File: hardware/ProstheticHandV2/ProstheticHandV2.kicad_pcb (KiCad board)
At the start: 2 copper layers, 130 x 70 mm, 94 parts, among them J1 BATT_CONNECTOR, J2 EMG_SENSOR_01, J3 EMG_SENSOR_02, J4 CONN_SERVO_02, J5 CONN_SERVO_01, J6 CONN_SERVO_03, SW1 DIP_SWITCH, SW2 BUTTON_01, SW3 BUTTON_02, U1 LM7805_TO220

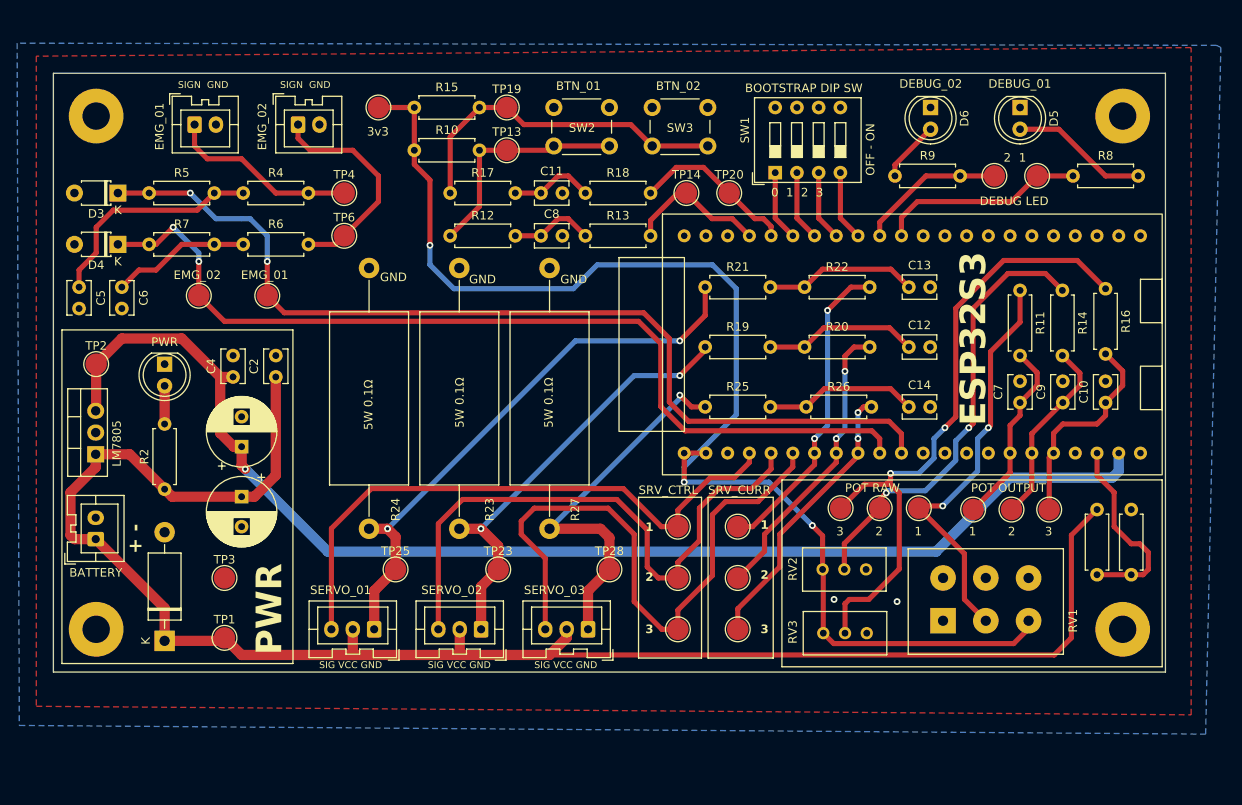
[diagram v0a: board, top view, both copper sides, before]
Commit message: Update PCB, sent to JLCPCB
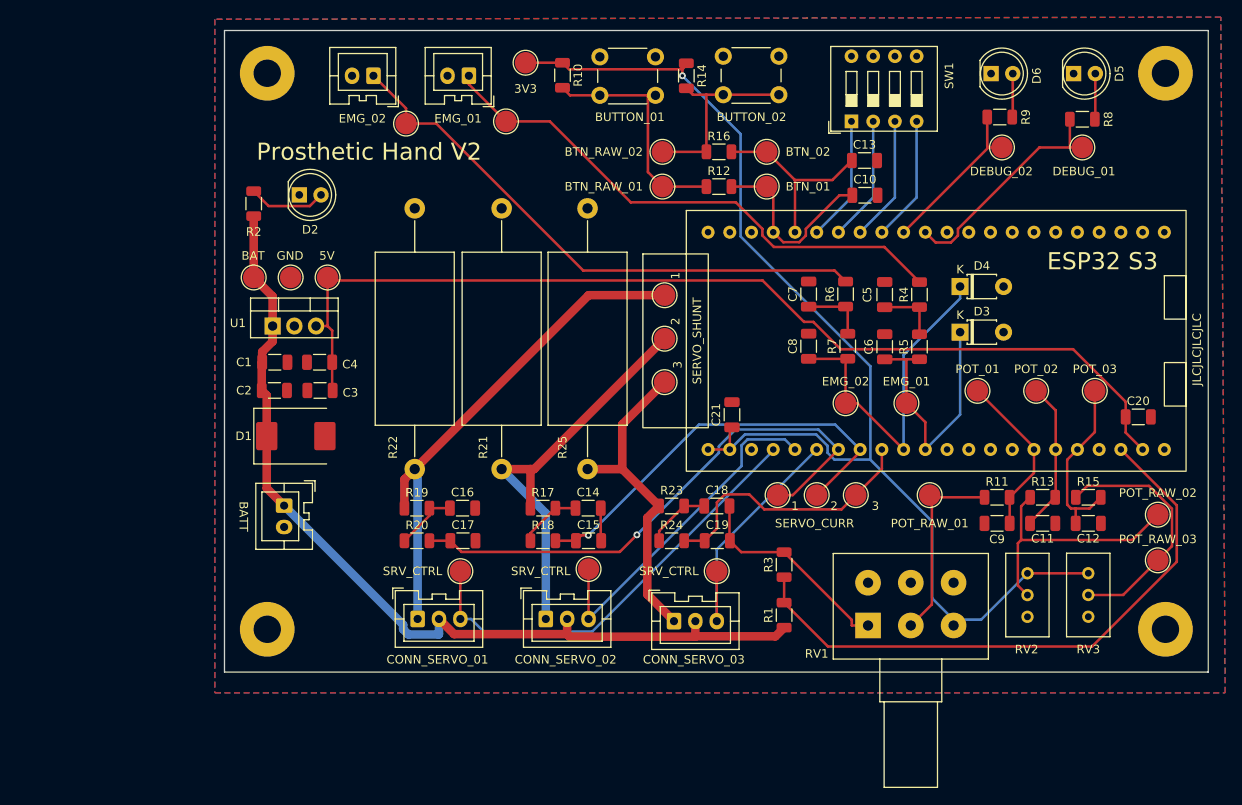
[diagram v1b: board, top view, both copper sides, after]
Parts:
- removed R26: 68k, Resistor_THT:R_Axial_DIN0207_L6.3mm_D2.5mm_P7.62mm_Horizontal
- removed R27: 0.1, Resistor_THT:R_Axial_DIN0922_L20.0mm_D9.0mm_P30.48mm_Horizontal
- added C15: 100nF, Capacitor_SMD:C_1206_3216Metric, F.Cu at (162.6, 104.6)
- added C16: 100nF, Capacitor_SMD:C_1206_3216Metric, F.Cu at (147.8, 100.8)
- added C17: 100nF, Capacitor_SMD:C_1206_3216Metric, F.Cu at (147.9, 104.6)
- added C18: 100nF, Capacitor_SMD:C_1206_3216Metric, F.Cu at (177.6, 100.6)
- added C19: 100nF, Capacitor_SMD:C_1206_3216Metric, F.Cu at (177.6, 104.6)
- added C20: 0.1uF, Capacitor_SMD:C_1206_3216Metric, F.Cu at (226.8, 90.2)
- added C21: 0.1uF, Capacitor_SMD:C_1206_3216Metric, F.Cu at (179.3, 89.9)
- C1, C3: value 470uF -> 1uF; footprint Capacitor_THT:CP_Radial_D8.0mm_P3.50mm -> Capacitor_SMD:C_1206_3216Metric
- C10, C9: value 68nF -> 0.1uF; footprint Capacitor_THT:C_Disc_D3.8mm_W2.6mm_P2.50mm -> Capacitor_SMD:C_1206_3216Metric
- C11, C12, C13: value 100nF -> 0.1uF; footprint Capacitor_THT:C_Disc_D3.8mm_W2.6mm_P2.50mm -> Capacitor_SMD:C_1206_3216Metric
- C14, C2, C4: footprint Capacitor_THT:C_Disc_D3.8mm_W2.6mm_P2.50mm -> Capacitor_SMD:C_1206_3216Metric
- C5, C6: value 0.1uF -> 1uF; footprint Capacitor_THT:C_Disc_D3.8mm_W2.6mm_P2.50mm -> Capacitor_SMD:C_1206_3216Metric
- C7: value 68nF -> 1uF; footprint Capacitor_THT:C_Disc_D3.8mm_W2.6mm_P2.50mm -> Capacitor_SMD:C_1206_3216Metric
- C8: value 100nF -> 1uF; footprint Capacitor_THT:C_Disc_D3.8mm_W2.6mm_P2.50mm -> Capacitor_SMD:C_1206_3216Metric
- D1: value FR207 -> SK36; footprint Diode_THT:D_DO-15_P12.70mm_Horizontal -> Diode_SMD:D_SMC
- R1: value 180k -> 4k7; footprint Resistor_THT:R_Axial_DIN0207_L6.3mm_D2.5mm_P7.62mm_Horizontal -> Resistor_SMD:R_1206_3216Metric
- R10, R12, R15, R2, R5, R7, R8, R9: footprint Resistor_THT:R_Axial_DIN0207_L6.3mm_D2.5mm_P7.62mm_Horizontal -> Resistor_SMD:R_1206_3216Metric
- R11, R14, R16: value 2k2 -> 10k; footprint Resistor_THT:R_Axial_DIN0207_L6.3mm_D2.5mm_P7.62mm_Horizontal -> Resistor_SMD:R_1206_3216Metric
- R13: value 33k -> 10k; footprint Resistor_THT:R_Axial_DIN0207_L6.3mm_D2.5mm_P7.62mm_Horizontal -> Resistor_SMD:R_1206_3216Metric
- R17: value 10k -> 1k; footprint Resistor_THT:R_Axial_DIN0207_L6.3mm_D2.5mm_P7.62mm_Horizontal -> Resistor_SMD:R_1206_3216Metric
- R18: value 33k -> 1k; footprint Resistor_THT:R_Axial_DIN0207_L6.3mm_D2.5mm_P7.62mm_Horizontal -> Resistor_SMD:R_1206_3216Metric
- R19: value 1k2 -> 1k; footprint Resistor_THT:R_Axial_DIN0207_L6.3mm_D2.5mm_P7.62mm_Horizontal -> Resistor_SMD:R_1206_3216Metric
- R20: value 68k -> 1k; footprint Resistor_THT:R_Axial_DIN0207_L6.3mm_D2.5mm_P7.62mm_Horizontal -> Resistor_SMD:R_1206_3216Metric
- R21, R25: value 1k2 -> 0.1; footprint Resistor_THT:R_Axial_DIN0207_L6.3mm_D2.5mm_P7.62mm_Horizontal -> Resistor_THT:R_Axial_DIN0922_L20.0mm_D9.0mm_P30.48mm_Horizontal
- R22: value 68k -> 0.1; footprint Resistor_THT:R_Axial_DIN0207_L6.3mm_D2.5mm_P7.62mm_Horizontal -> Resistor_THT:R_Axial_DIN0922_L20.0mm_D9.0mm_P30.48mm_Horizontal
- R23, R24: value 0.1 -> 1k; footprint Resistor_THT:R_Axial_DIN0922_L20.0mm_D9.0mm_P30.48mm_Horizontal -> Resistor_SMD:R_1206_3216Metric
- R3: value 47k -> 1k; footprint Resistor_THT:R_Axial_DIN0207_L6.3mm_D2.5mm_P7.62mm_Horizontal -> Resistor_SMD:R_1206_3216Metric
- R4, R6: value 330k -> 10k; footprint Resistor_THT:R_Axial_DIN0207_L6.3mm_D2.5mm_P7.62mm_Horizontal -> Resistor_SMD:R_1206_3216Metric
- moved D3 99.8 mm to (206.0, 80.3), turned to 0 degrees
- moved D4 98.6 mm to (206.0, 74.9), turned to 0 degrees
- moved C5 94.2 mm to (197.2, 75.9), turned to 90 degrees
- moved R5 91.8 mm to (201.2, 82.0), turned to 90 degrees
- moved R15 91.0 mm to (221.0, 99.6)
- moved C6 89.4 mm to (197.2, 82.0), turned to 90 degrees
- moved R7 82.5 mm to (192.9, 81.9), turned to 90 degrees
- moved R4 79.9 mm to (201.2, 75.9), turned to 90 degrees
- moved TP7 76.6 mm to (192.6, 88.6)
- moved TP5 75.8 mm to (199.7, 88.6)
- moved R6 70.7 mm to (192.6, 75.8), turned to 90 degrees
- moved C11 70.2 mm to (215.6, 102.6)
- moved R13 61.6 mm to (215.6, 99.6)
- moved R20 50.7 mm to (142.5, 104.6)
- moved R14 50.6 mm to (174.0, 50.3)
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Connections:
- C10 pad 1: POT_03 -> BUTTON_01
- C11 pad 1: Net-(C11-Pad1) -> POT_02
- C12 pad 1: Net-(C12-Pad1) -> POT_03
- C13 pad 1: Net-(C13-Pad1) -> BUTTON_02
- C6 pad 1: Net-(C6-Pad1) -> EMG_SENSOR_01
- C7 pad 1: POT_01 -> Net-(C7-Pad1)
- C8 pad 1: Net-(C8-Pad1) -> EMG_SENSOR_02
- C9 pad 1: POT_02 -> POT_01
- R12 pad 2: Net-(C8-Pad1) -> BUTTON_01
- R13 pad 1: Net-(C8-Pad1) -> Net-(R13-Pad1)
- R13 pad 2: BUTTON_01 -> POT_02
- R14 pad 1: Net-(R14-Pad1) -> +3V3
- R14 pad 2: POT_02 -> Net-(R14-Pad2)
- R15 pad 1: +3V3 -> Net-(R15-Pad1)
- R15 pad 2: Net-(R15-Pad2) -> POT_03
- R16 pad 1: Net-(R16-Pad1) -> Net-(R14-Pad2)
- R16 pad 2: POT_03 -> BUTTON_02
- R17 pad 1: Net-(R15-Pad2) -> Net-(J4-Pin_1)
- R17 pad 2: Net-(C11-Pad1) -> Net-(C14-Pad1)
- R18 pad 1: Net-(C11-Pad1) -> Net-(C14-Pad1)
- R18 pad 2: BUTTON_02 -> SERVO_CURR_02
- R19 pad 1: Net-(J4-Pin_1) -> Net-(J5-Pin_1)
- R19 pad 2: Net-(C12-Pad1) -> Net-(C16-Pad1)
- R20 pad 1: Net-(C12-Pad1) -> Net-(C16-Pad1)
- R20 pad 2: SERVO_CURR_02 -> SERVO_CURR_01
- R21 pad 1: Net-(J5-Pin_1) -> Net-(J4-Pin_1)
- R21 pad 2: Net-(C13-Pad1) -> GND
- R22 pad 1: Net-(C13-Pad1) -> Net-(J5-Pin_1)
- R22 pad 2: SERVO_CURR_01 -> GND
- R23 pad 1: Net-(J4-Pin_1) -> Net-(J6-Pin_1)
- R23 pad 2: GND -> Net-(C18-Pad1)
- R24 pad 1: Net-(J5-Pin_1) -> Net-(C18-Pad1)
- R24 pad 2: GND -> SERVO_CURR_03
- R25 pad 2: Net-(C14-Pad1) -> GND
- R6 pad 1: Net-(C6-Pad1) -> Net-(C7-Pad1)
- R7 pad 2: Net-(C6-Pad1) -> Net-(C7-Pad1)
- RV2 pad 2: Net-(R14-Pad1) -> Net-(R13-Pad1)
- RV3 pad 2: Net-(R16-Pad1) -> Net-(R15-Pad1)
- SW3 pad 2: Net-(R15-Pad2) -> Net-(R14-Pad2)
- TP15 pad 1: Net-(R14-Pad1) -> Net-(R13-Pad1)
- TP17 pad 1: Net-(R16-Pad1) -> Net-(R15-Pad1)
- TP19 pad 1: Net-(R15-Pad2) -> Net-(R14-Pad2)
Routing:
- net +BATT: track 198.6 -> 108.0 mm
- net EMG_SENSOR_01: track 114.0 -> 30.9 mm, vias 2 -> 0
- net Net-(R16-Pad1): track 75.9 -> 0.00 mm, vias 2 -> 0
- net EMG_SENSOR_02: track 109.2 -> 40.6 mm, vias 2 -> 0
- net Net-(R14-Pad1): track 52.2 -> 0.00 mm, vias 2 -> 0
- net BATT_SENSE: track 22.9 -> 70.9 mm
- net Net-(J2-Pin_1): track 22.3 -> 63.7 mm
- net SERVO_CONTROL_03: track 71.6 -> 30.7 mm
- net Net-(J3-Pin_1): track 26.1 -> 66.2 mm
- net Net-(R15-Pad2): track 40.0 -> 0.00 mm
- net Net-(R13-Pad1): track 0.00 -> 29.7 mm
- net Net-(R15-Pad1): track 0.00 -> 29.4 mm
- net +5V: track 149.2 -> 120.4 mm, vias 1 -> 0
- net SERVO_CONTROL_02: track 69.2 -> 40.6 mm
- net GND: track 0.00 -> 28.6 mm, vias 2 -> 0
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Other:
- board size 130 x 70 mm -> 115 x 75 mm
- board text added: "3V3"
- board text added: "5V"
- board text added: "BAT"
- board text added: "BATT"
- board text added: "BTN_RAW_01"
- board text added: "BTN_RAW_02"
- board text added: "BUTTON_01"
- board text added: "BUTTON_02"
- board text added: "CONN_SERVO_01"
- board text added: "CONN_SERVO_02"
- board text added: "CONN_SERVO_03"
- board text added: "ESP32 S3"
- board text added: "JLCJLCJLCJLC"
- board text added: "POT_01"
- board text added: "POT_02"
- board text added: "POT_03"
- board text added: "POT_RAW_01"
- board text added: "POT_RAW_02"
- board text added: "POT_RAW_03"
- board text added: "Prosthetic Hand V2"
- board text added: "SERVO_CURR"
- board text added: "SERVO_SHUNT"
- board text removed: "+ -"
- board text removed: "0 1 2 3"
- board text removed: "3v3"
- board text removed: "5W 0.1Ω"
- board text removed: "BATTERY"
- board text removed: "BOOTSTRAP DIP SW"
- board text removed: "DEBUG LED"
- board text removed: "ESP32S3"
- board text removed: "LM7805"
- board text removed: "OFF - ON"
- board text removed: "POT OUTPUT"
- board text removed: "POT RAW"
- board text removed: "PWR"
- board text removed: "SERVO_01"
- board text removed: "SERVO_02"
- board text removed: "SERVO_03"
- board text removed: "SIG VCC GND"
- board text removed: "SIGN GND"
- board text removed: "SRV_CURR"
